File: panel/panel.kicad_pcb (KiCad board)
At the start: 2 copper layers, 101.3 x 128.4 mm, 37 parts

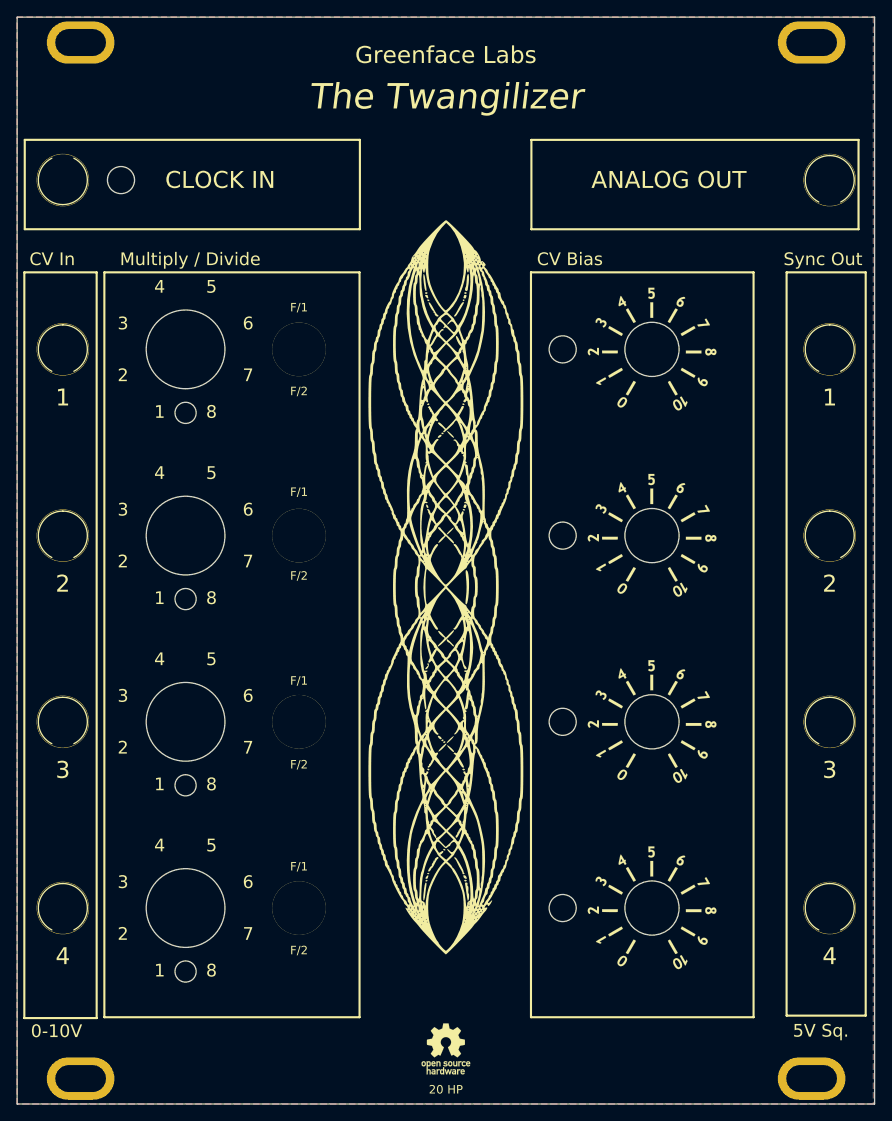
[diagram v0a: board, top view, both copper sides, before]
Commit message: v1.0
Docs still need work.
Oscillators.sch not used. Saved just in case.
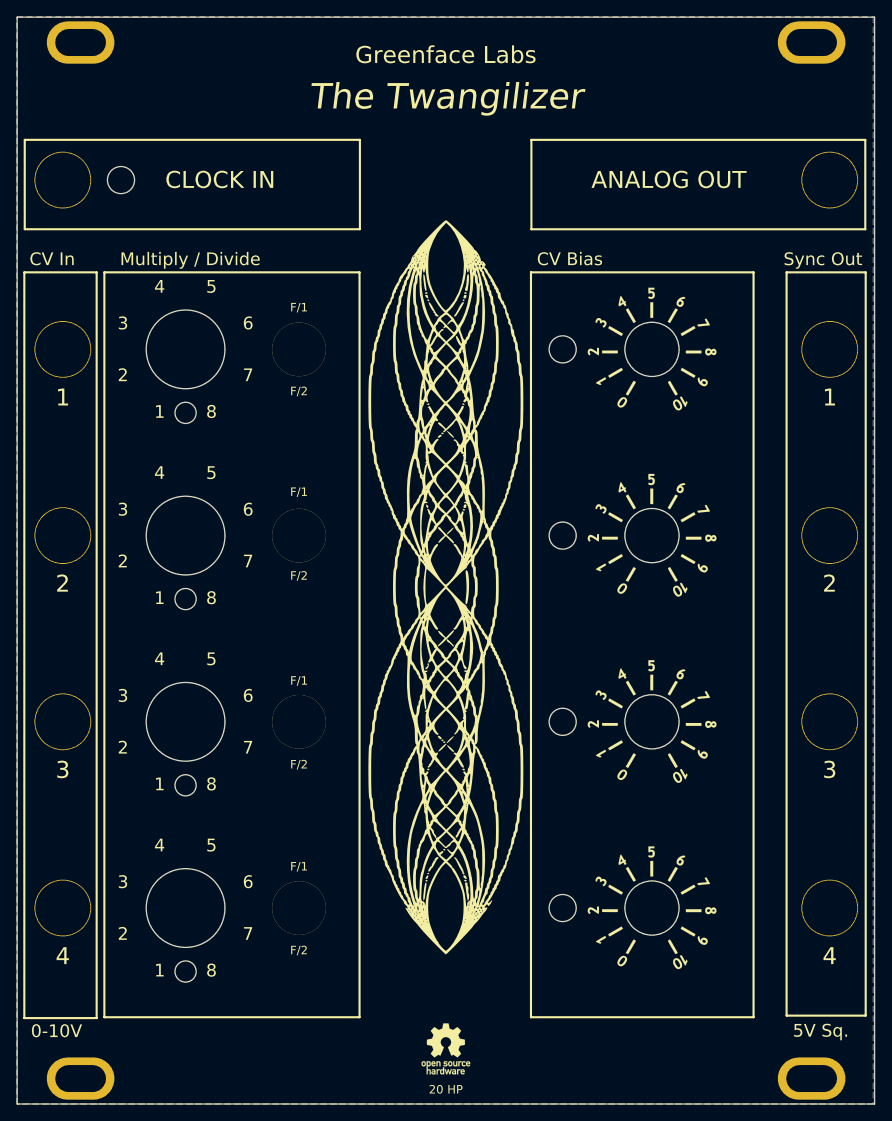
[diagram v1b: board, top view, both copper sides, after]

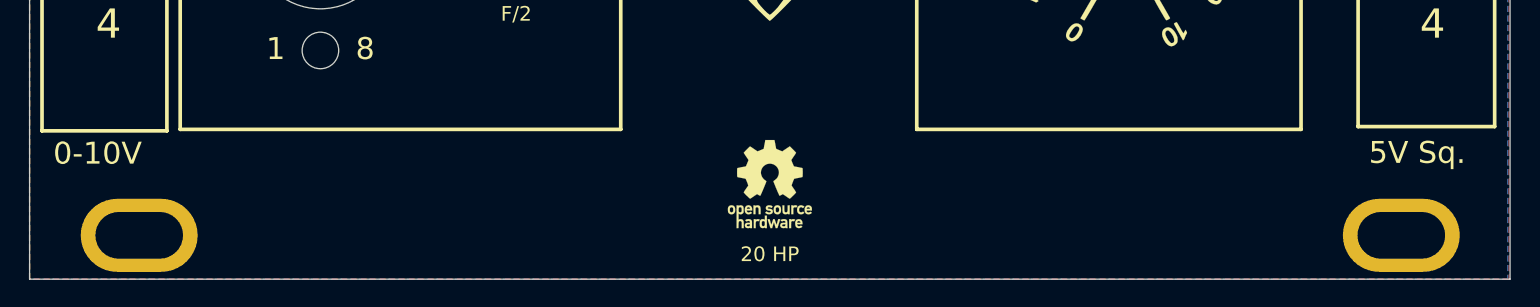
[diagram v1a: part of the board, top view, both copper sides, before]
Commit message: Work in progress
Adds User Manual
Changes CV range to 0 - 8V
Adds spice vactrol test circuit.
Adds VCA spice study
Updates other spice and excel files.
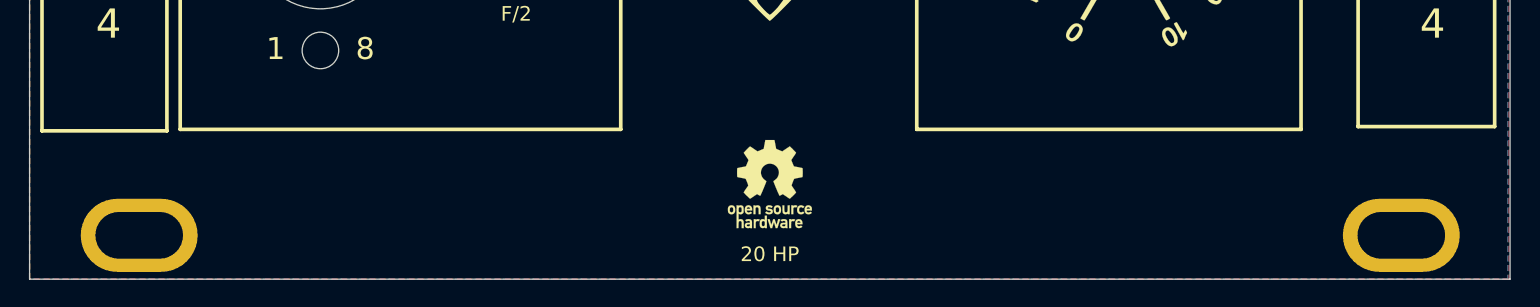
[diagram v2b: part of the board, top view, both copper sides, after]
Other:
- board text removed: "0-10V"
- board text removed: "5V Sq."
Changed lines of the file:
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@@
   (title_block
     (title "Twangilizer Panel")
-    (rev "1.1")
+    (rev "1.2")
   )
   (layers
@@
     (effects (font (size 2 2) (thickness 0.3)))
   )
-  (gr_text "0-10V" (at 44.65 150.55) (layer "F.SilkS")
-    (effects (font (size 1.5 1.5) (thickness 0.2)))
-  )
   (gr_text "1" (at 45.4 75.7) (layer "F.SilkS")
     (effects (font (size 2 2) (thickness 0.3)))
@@
     (effects (font (size 1.5 1.5) (thickness 0.3)))
   )
-  (gr_text "5V Sq." (at 134.95 150.5) (layer "F.SilkS")
-    (effects (font (size 1.5 1.5) (thickness 0.3)))
-  )

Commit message: v2.0
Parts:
- added H17: MountingHole, panel:3mmLED, F.Cu at (128.7, 51.1)
- moved H16 2.11 mm to (52.8, 51.1), turned to 90 degrees
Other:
- board text added: "clip"
